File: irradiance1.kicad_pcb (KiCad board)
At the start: 2 copper layers, 61 x 75 mm, 30 parts, among them J0 Conn_01x06, J4 CAN_In, J5 CAN_Out, J6 Battery, U1 ADM3055E, U2 Nucleo_L432KC, U7 CDSOT23-T24CAN

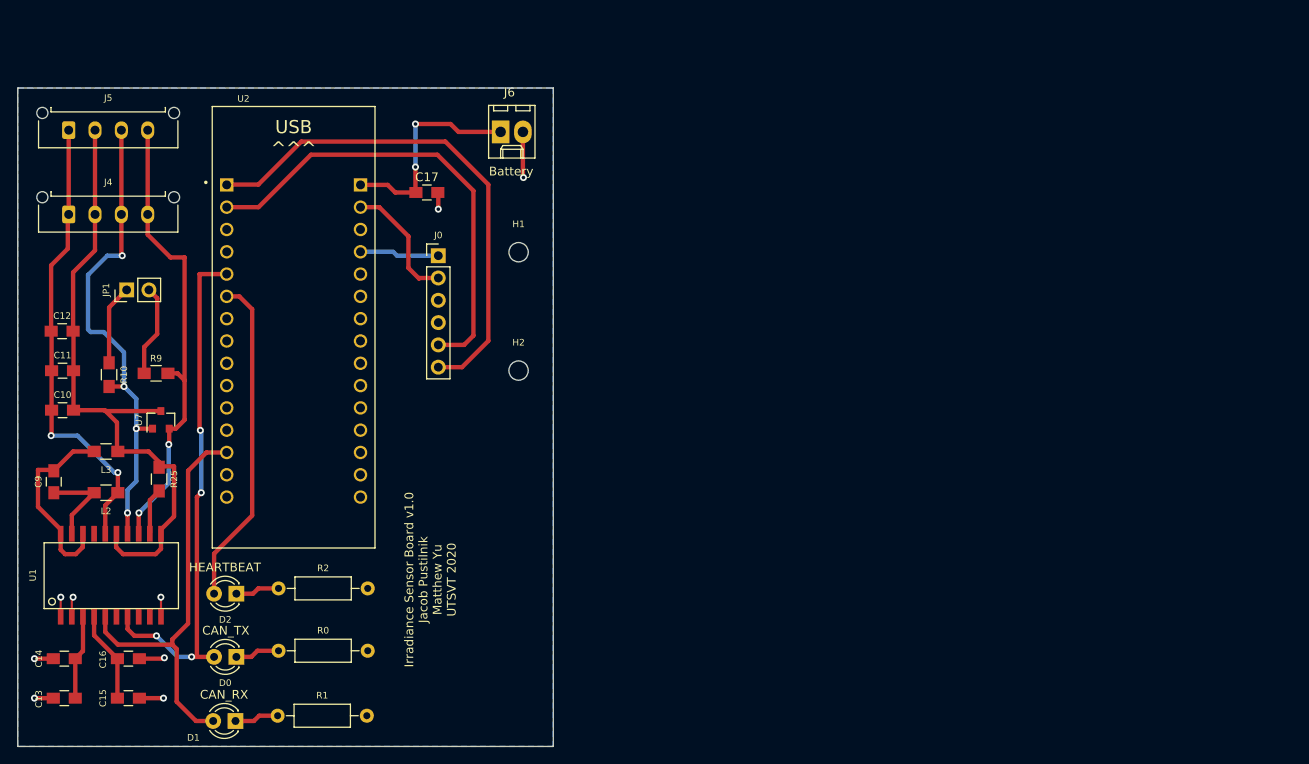
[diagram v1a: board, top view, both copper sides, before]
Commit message: Initial commit of board revamp: - Reduced the size of the components to 0402s and 0603s to save space on the board - Modified the schematic to make it easier to look at and interpret - Added the TSL25911FN sensor - Added new symbols and footprints for the new components - Added links to the datasheets for the new components
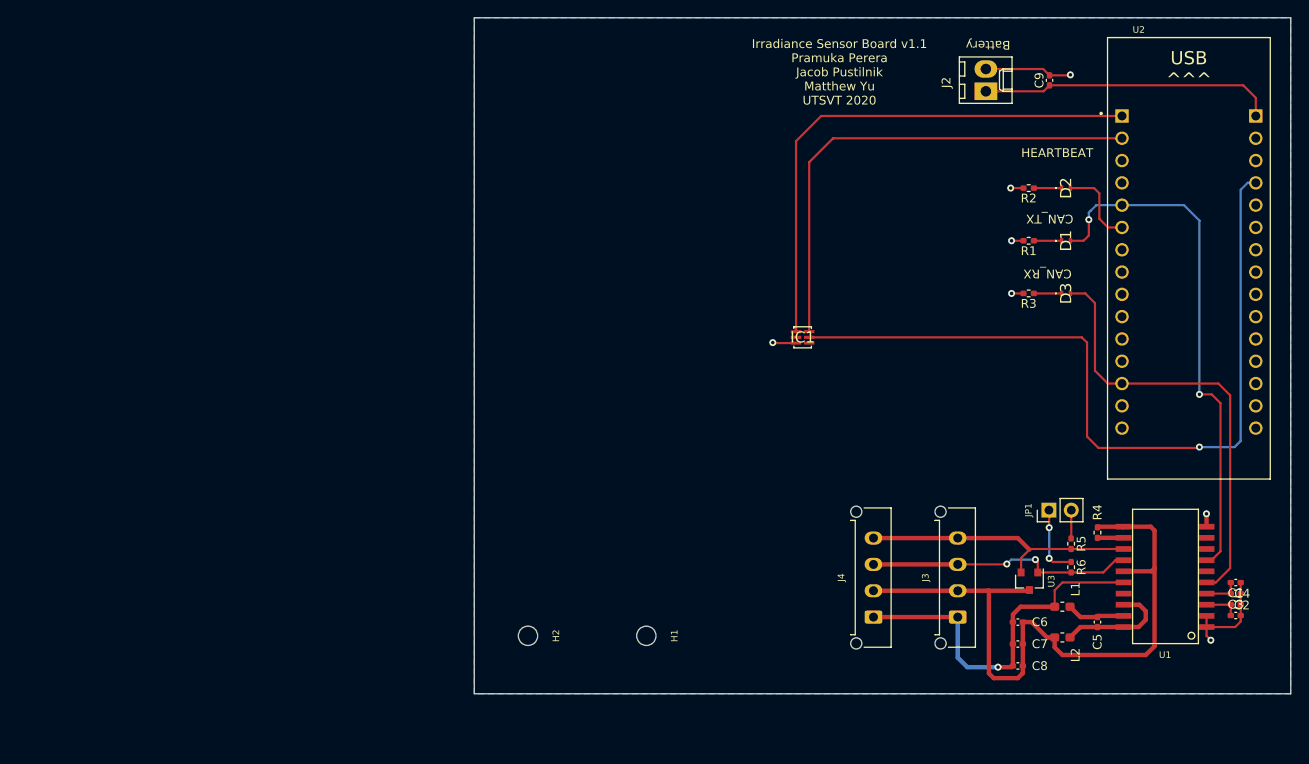
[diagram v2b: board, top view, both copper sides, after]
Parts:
- removed J0: Conn_01x06, Connector_PinHeader_2.54mm:PinHeader_1x06_P2.54mm_Vertical
- removed R0: 330, Resistors_THT:R_Axial_DIN0207_L6.3mm_D2.5mm_P10.16mm_Horizontal
- added IC1: TSL25911FN, irradianceboard:TSL25911FN, F.Cu at (116.4, 96.4)
- added R3: 330, Resistor_SMD:R_0402_1005Metric_Pad0.72x0.64mm_HandSolder, F.Cu at (142.2, 91.4)
- C1: renamed from C13; footprint Capacitors_SMD:C_0805_HandSoldering -> Capacitor_SMD:C_0402_1005Metric_Pad0.74x0.62mm_HandSolder
- C2: renamed from C14; footprint Capacitors_SMD:C_0805_HandSoldering -> Capacitor_SMD:C_0402_1005Metric_Pad0.74x0.62mm_HandSolder
- C3: renamed from C15; footprint Capacitors_SMD:C_0805_HandSoldering -> Capacitor_SMD:C_0402_1005Metric_Pad0.74x0.62mm_HandSolder
- C4: renamed from C16; footprint Capacitors_SMD:C_0805_HandSoldering -> Capacitor_SMD:C_0402_1005Metric_Pad0.74x0.62mm_HandSolder
- C5: renamed from C9; footprint Capacitors_SMD:C_0805_HandSoldering -> Capacitor_SMD:C_0402_1005Metric_Pad0.74x0.62mm_HandSolder
- C6: renamed from C10; footprint Capacitors_SMD:C_0805_HandSoldering -> Capacitor_SMD:C_0402_1005Metric_Pad0.74x0.62mm_HandSolder
- C7: renamed from C11; footprint Capacitors_SMD:C_0805_HandSoldering -> Capacitor_SMD:C_0402_1005Metric_Pad0.74x0.62mm_HandSolder
- C8: renamed from C12; footprint Capacitors_SMD:C_0805_HandSoldering -> Capacitor_SMD:C_0402_1005Metric_Pad0.74x0.62mm_HandSolder
- C9: renamed from C17; footprint Capacitors_SMD:C_0805_HandSoldering -> Capacitor_SMD:C_0402_1005Metric_Pad0.74x0.62mm_HandSolder
- D1: renamed from D0; footprint LEDs:LED_D3.0mm -> irradianceboard:SM0402GC
- D2: footprint LEDs:LED_D3.0mm -> irradianceboard:SM0402GC
- D3: renamed from D1; footprint LEDs:LED_D3.0mm -> irradianceboard:SM0402GC
- L1: renamed from L2; footprint Inductors_SMD:L_0805_HandSoldering -> Inductor_SMD:L_0603_1608Metric_Pad1.05x0.95mm_HandSolder
- L2: renamed from L3; footprint Inductors_SMD:L_0805_HandSoldering -> Inductor_SMD:L_0603_1608Metric_Pad1.05x0.95mm_HandSolder
- R1, R2: footprint Resistors_THT:R_Axial_DIN0207_L6.3mm_D2.5mm_P10.16mm_Horizontal -> Resistor_SMD:R_0402_1005Metric_Pad0.72x0.64mm_HandSolder
- R4: renamed from R25; footprint Resistors_SMD:R_0805_HandSoldering -> Resistor_SMD:R_0402_1005Metric_Pad0.72x0.64mm_HandSolder
- R5: renamed from R9; footprint Resistors_SMD:R_0805_HandSoldering -> Resistor_SMD:R_0402_1005Metric_Pad0.72x0.64mm_HandSolder
- R6: renamed from R10; footprint Resistors_SMD:R_0805_HandSoldering -> Resistor_SMD:R_0402_1005Metric_Pad0.72x0.64mm_HandSolder
- moved C1 133.9 mm to (165.7, 126.8), turned to 0 degrees
- moved C2 133.5 mm to (165.7, 128.1), turned to 0 degrees
- moved C3 126.7 mm to (165.7, 125.6)
- moved C4 126.4 mm to (165.7, 124.3)
- moved U1 120.1 mm to (157.7, 123.7), turned to 180 degrees
- moved C5 120.0 mm to (150.0, 128.8), turned to -90 degrees
- moved C8 115.4 mm to (140.9, 133.8)
- moved C7 113.2 mm to (140.9, 131.3)
- moved R6 111.8 mm to (147.0, 122.6)
- moved C6 111.5 mm to (140.9, 128.8)
- moved J3 111.2 mm to (134.1, 128.3), turned to 90 degrees
- moved L2 111.0 mm to (146.0, 130.6), turned to 0 degrees
- moved L1 109.7 mm to (146.0, 127.1), turned to 0 degrees
- moved JP1 108.0 mm to (144.5, 116.1)
- moved J4 107.1 mm to (124.5, 128.3), turned to 90 degrees
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- renumbered J6 to J2, J4 to J3, J5 to J4, U7 to U3
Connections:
- D1 pad 1: Net-(D0-Pad1) -> Net-(D1-Pad1)
- D3 pad 1: Net-(D1-Pad1) -> Net-(D3-Pad1)
- U1 pad 17: (no net) -> unconnected-(U1-Pad17)
- U1 pad 6: (no net) -> unconnected-(U1-Pad6)
- U1 pad 8: (no net) -> unconnected-(U1-Pad8)
- U1 pad 9: (no net) -> unconnected-(U1-Pad9)
- U2 pad 10: (no net) -> unconnected-(U2-Pad10)
- U2 pad 11: (no net) -> unconnected-(U2-Pad11)
- U2 pad 12: (no net) -> unconnected-(U2-Pad12)
- U2 pad 14: (no net) -> unconnected-(U2-Pad14)
- U2 pad 15: (no net) -> unconnected-(U2-Pad15)
- U2 pad 16: (no net) -> unconnected-(U2-Pad16)
- U2 pad 17: (no net) -> unconnected-(U2-Pad17)
- U2 pad 18: (no net) -> unconnected-(U2-Pad18)
- U2 pad 19: (no net) -> unconnected-(U2-Pad19)
- U2 pad 20: (no net) -> unconnected-(U2-Pad20)
- U2 pad 21: (no net) -> unconnected-(U2-Pad21)
- U2 pad 22: (no net) -> unconnected-(U2-Pad22)
- U2 pad 23: (no net) -> unconnected-(U2-Pad23)
- U2 pad 24: (no net) -> unconnected-(U2-Pad24)
- U2 pad 25: (no net) -> unconnected-(U2-Pad25)
- U2 pad 26: (no net) -> unconnected-(U2-Pad26)
- U2 pad 27: vin -> VDD
- U2 pad 28: (no net) -> unconnected-(U2-Pad28)
- U2 pad 29: Net-(J0-Pad2) -> GND
- U2 pad 3: (no net) -> unconnected-(U2-Pad3)
- U2 pad 4: (no net) -> unconnected-(U2-Pad4)
- U2 pad 7: (no net) -> unconnected-(U2-Pad7)
- U2 pad 8: (no net) -> unconnected-(U2-Pad8)
- U2 pad 9: (no net) -> unconnected-(U2-Pad9)
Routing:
- net VDD: track 0.00 -> 91.6 mm, vias 0 -> 1
- net Net-(D2-Pad2): track 37.7 -> 9.44 mm
- net Net-(J3-Pad3): track 55.8 -> 30.6 mm, vias 4 -> 2
- net Net-(J3-Pad4): track 53.5 -> 32.1 mm, vias 2 -> 0
- net Net-(J0-Pad2): track 14.4 -> 0.00 mm
- net Net-(C6-Pad1): track 52.6 -> 42.1 mm, vias 2 -> 1
- net +9VA: track 24.6 -> 33.7 mm, vias 2 -> 0
- net vin: track 9.04 -> 0.00 mm
- net Net-(C5-Pad2): track 22.1 -> 13.3 mm
- net Net-(JP1-Pad2): track 10.5 -> 3.24 mm
- net +3V3: track 10.4 -> 4.01 mm
- net GND: track 23.8 -> 29.8 mm, vias 9 -> 7
- net Net-(C6-Pad2): track 73.0 -> 78.9 mm
- net +5V: track 9.64 -> 4.02 mm
- net Net-(D0-Pad1): track 5.09 -> 0.00 mm
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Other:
- board size 61 x 75 mm -> 93 x 77 mm
- net class Default removed
- board text added: "Irradiance Sensor Board v1.1 Pramuka Perera Jacob Pustilnik Matthew Yu UTSVT 2020"
- board text added: "Note that the total trace length between the ends of the low ESR capacitors and the input power supply pins, VCC, VIO, VISOIN, and VISOOUT, must not exceed 2 mm."
- board text removed: "Irradiance Sensor Board v1.0 Jacob Pustilnik Matthew Yu UTSVT 2020"

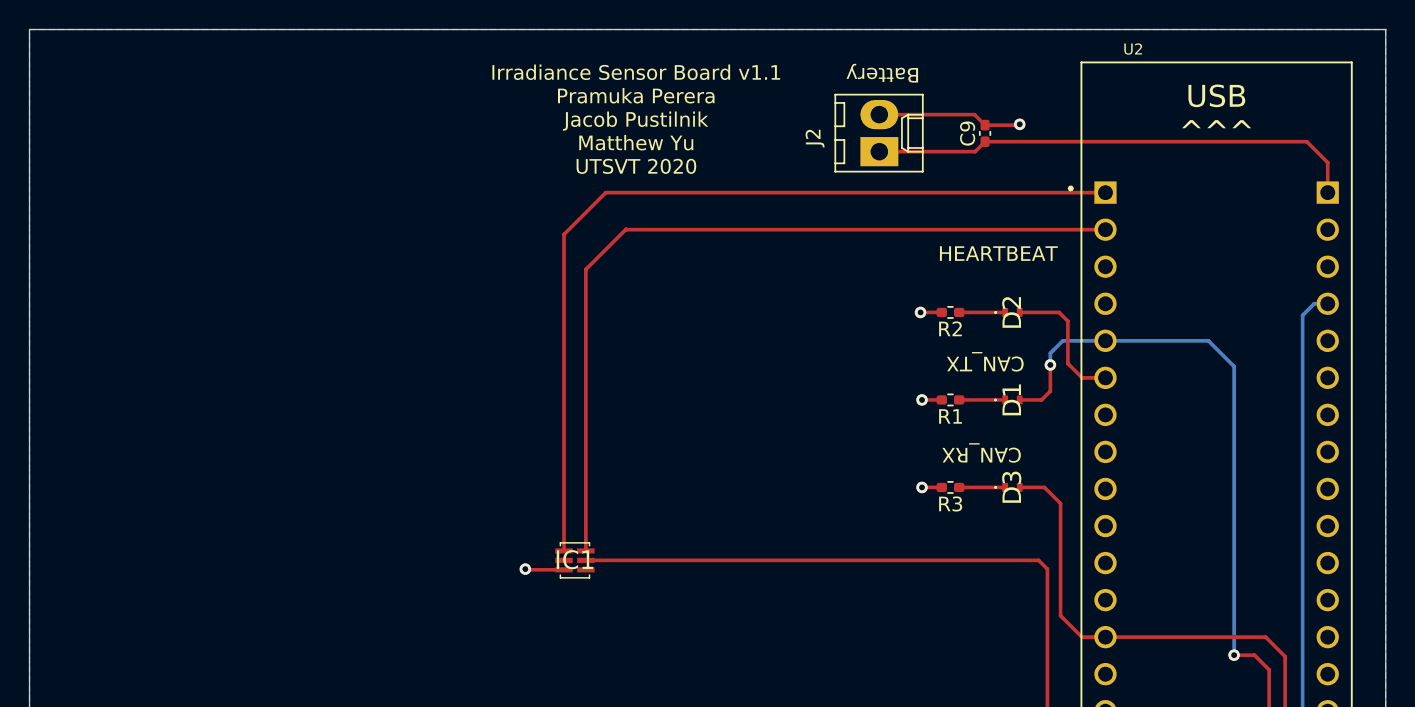
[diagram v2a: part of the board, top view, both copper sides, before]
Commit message: Made updates based on feedback: - Added series schottky diode for reverse polarity protection at J2 - Added cap and open-drain resistors for light sensor (IC1) - Connected grounds on Nucleo - Added 10 uF cap at J2 - Other small changes
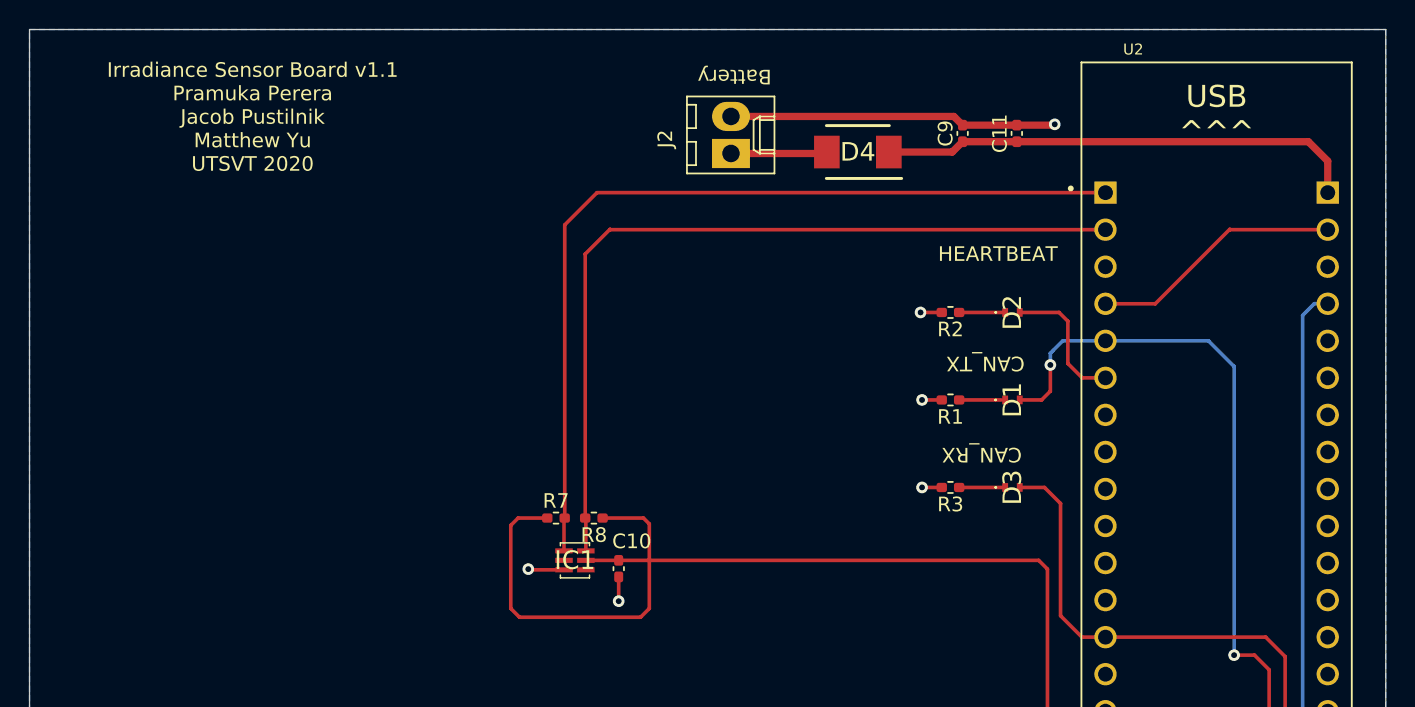
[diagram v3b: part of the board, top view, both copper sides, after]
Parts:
- added C10: 1u, Capacitor_SMD:C_0402_1005Metric_Pad0.74x0.62mm_HandSolder, F.Cu at (119.4, 97.0)
- added C11: 10u, Capacitor_SMD:C_0402_1005Metric_Pad0.74x0.62mm_HandSolder, F.Cu at (146.7, 67.1)
- added D4: D_Schottky, irradianceboard:SODFL5436X110N, F.Cu at (135.8, 68.4)
- added R7: 1.5k, Resistor_SMD:R_0402_1005Metric_Pad0.72x0.64mm_HandSolder, F.Cu at (115.1, 93.5)
- added R8: 1.5k, Resistor_SMD:R_0402_1005Metric_Pad0.72x0.64mm_HandSolder, F.Cu at (117.7, 93.5)
- moved J2 10.2 mm to (127.1, 68.5)
- moved C9 1.54 mm to (143.0, 67.1)
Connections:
- J2 pad 1: +9VA -> Net-(J2-Pad1)
- U2 pad 4: unconnected-(U2-Pad4) -> GND
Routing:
- net GND: track 29.8 -> 61.2 mm, vias 7 -> 8
- net VDD: track 91.6 -> 119.2 mm
- net Net-(J2-Pad1): track 0.00 -> 6.62 mm
- net I2C_SDA: track 56.1 -> 56.8 mm
- net +9VA: track 33.7 -> 33.1 mm
